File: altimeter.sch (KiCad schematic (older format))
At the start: 42 parts, among them Q101 DMG2301L, Q102 NTR4003NT1G, Q103 SISS05dn, U1 LMV331, U101 STM32F302CCTx, U102 S25FL512SAGMFIR11, U103 AIS2120SXTR, U104 MIC5219-3.3YM5, U105 LF50_TO252, U106 BMI088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

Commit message: first prototyp order
Signed-off-by: Thomas Schmid <tom@binary-kitchen.de>
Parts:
- removed D102: D_Zener, symbol Device:D_Zener
- added D102: LED, LED_SMD:LED_0603_1608Metric, symbol Device:LED
- R105: value 100k -> 680; Mouser_Link https://www.mouser.de/ProductDetail/Vishay-Dale/CRCW0402100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 -> https://www.mouser.de/ProductDetail/Vishay-Dale/CRCW0402680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; Parnumber CRCW0402100KFKEDC -> CRCW0402680RFKEDC
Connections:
- net +3V3: now also R105.2
- net GND: now also Q103.4 (G), D102.1 (K); no longer R105.2
- net at R105.1: now also D102.2 (A); no longer Q103.4 (G)
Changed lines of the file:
@@
 Connection ~ 7000 3200
 Wire Wire Line
-	8000 900  8000 1150
+	8000 900  8000 1050
 NoConn ~ 6300 3000
 NoConn ~ 6300 2800
@@
 Wire Wire Line
 	7550 1650 7550 1700
-Wire Wire Line
-	7550 1700 7400 1700
 $Comp
 L power:GND #PWR0164
 U 1 1 5D749A10
-P 7050 2550
-F 0 "#PWR0164" H 7050 2300 50  0001 C CNN
-F 1 "GND" H 7055 2377 50  0000 C CNN
-F 2 "" H 7050 2550 50  0001 C CNN
-F 3 "" H 7050 2550 50  0001 C CNN
-	1    7050 2550
-	1    0    0    -1
-$EndComp
-$Comp
-L Device:D_Zener D102
-U 1 1 5D74B84D
-P 7400 1900
-F 0 "D102" V 7446 1821 50  0000 R CNN
-F 1 "D_Zener" V 7355 1821 50  0000 R CNN
-F 2 "" H 7400 1900 50  0001 C CNN
-F 3 "~" H 7400 1900 50  0001 C CNN
-	1    7400 1900
-	0    -1   -1   0
-$EndComp
-$Comp
-L Device:R R105
-U 1 1 5D74CCF3
-P 7050 2300
-F 0 "R105" H 7120 2346 50  0000 L CNN
-F 1 "100k" H 7120 2255 50  0000 L CNN
-F 2 "Resistor_SMD:R_0402_1005Metric" V 6980 2300 50  0001 C CNN
-F 3 "~" H 7050 2300 50  0001 C CNN
-F 4 "https://www.mouser.de/ProductDetail/Vishay-Dale/CRCW0402100KFKED?qs=sGAEpiMZZMu61qfTUdNhG2DpbjADlD3GqPf2An0kBCw%3D" H 7050 2300 50  0001 C CNN "Mouser_Link"
-F 5 "CRCW0402100KFKEDC" H 7050 2300 50  0001 C CNN "Parnumber"
-	1    7050 2300
-	1    0    0    -1
-$EndComp
-Wire Wire Line
-	7050 2000 7050 2100
-Wire Wire Line
-	7050 2100 7400 2100
-Wire Wire Line
-	7400 2100 7400 2050
-Wire Wire Line
-	7400 1750 7400 1700
-Connection ~ 7400 1700
-Wire Wire Line
-	7400 1700 7250 1700
-Wire Wire Line
-	7050 2550 7050 2450
-Wire Wire Line
-	7050 2150 7050 2100
-Connection ~ 7050 2100
+P 7050 2150
+F 0 "#PWR0164" H 7050 1900 50  0001 C CNN
+F 1 "GND" H 7055 1977 50  0000 C CNN
+F 2 "" H 7050 2150 50  0001 C CNN
+F 3 "" H 7050 2150 50  0001 C CNN
+	1    7050 2150
+	1    0    0    -1
+$EndComp
 $Comp
 L altimeter:SI7149ADP Q103
@@
 $EndComp
 $Comp
-L power:VPP #PWR?
+L power:VPP #PWR0113
 U 1 1 5D715463
 P 2000 5150
-F 0 "#PWR?" H 2000 5000 50  0001 C CNN
+F 0 "#PWR0113" H 2000 5000 50  0001 C CNN
 F 1 "VPP" H 2015 5323 50  0000 C CNN
 F 2 "" H 2000 5150 50  0001 C CNN
@@
 $EndComp
 $Comp
-L power:VPP #PWR?
+L power:VPP #PWR0115
 U 1 1 5D715F7E
 P 9350 3300
-F 0 "#PWR?" H 9350 3150 50  0001 C CNN
+F 0 "#PWR0115" H 9350 3150 50  0001 C CNN
 F 1 "VPP" H 9365 3473 50  0000 C CNN
 F 2 "" H 9350 3300 50  0001 C CNN
@@
 $EndComp
 $Comp
-L power:VPP #PWR?
+L power:VPP #PWR0132
 U 1 1 5D7169CC
 P 8750 1000
-F 0 "#PWR?" H 8750 850 50  0001 C CNN
+F 0 "#PWR0132" H 8750 850 50  0001 C CNN
 F 1 "VPP" H 8765 1173 50  0000 C CNN
 F 2 "" H 8750 1000 50  0001 C CNN
@@
 	1    0    0    -1
 $EndComp
+Wire Wire Line
+	7050 2000 7050 2150
+Wire Wire Line
+	7250 1700 7550 1700
+$Comp
+L Device:R R105
+U 1 1 5D7330BE
+P 7250 1200
+F 0 "R105" V 7043 1200 50  0000 C CNN
+F 1 "680" V 7134 1200 50  0000 C CNN
+F 2 "Resistor_SMD:R_0402_1005Metric" V 7180 1200 50  0001 C CNN
+F 3 "~" H 7250 1200 50  0001 C CNN
+F 4 "https://www.mouser.de/ProductDetail/Vishay-Dale/CRCW0402680RFKED?qs=sGAEpiMZZMu61qfTUdNhG2DpbjADlD3GyuaBeN1cc%2FA%3D" H 7250 1200 50  0001 C CNN "Mouser_Link"
+F 5 "CRCW0402680RFKEDC" H 7250 1200 50  0001 C CNN "Parnumber"
+	1    7250 1200
+	0    1    1    0
+$EndComp
+$Comp
+L Device:LED D102
+U 1 1 5D733512
+P 7650 1200
+F 0 "D102" H 7643 945 50  0000 C CNN
+F 1 "LED" H 7643 1036 50  0000 C CNN
+F 2 "LED_SMD:LED_0603_1608Metric" H 7650 1200 50  0001 C CNN
+F 3 "~" H 7650 1200 50  0001 C CNN
+F 4 "https://www.mouser.de/ProductDetail/Kingbright/APTD1608LSURCK?qs=sGAEpiMZZMseGfSY3csMkdgyOOAg6kv2cxPgKHWlbm1IZYxSy1q3mw%3D%3D" H 7650 1200 50  0001 C CNN "Mouser_Link"
+F 5 "APTD1608LSURCK" H 7650 1200 50  0001 C CNN "Parnumber"
+	1    7650 1200
+	-1   0    0    1
+$EndComp
+Wire Wire Line
+	7400 1200 7500 1200
+Wire Wire Line
+	7800 1200 7900 1200
+Wire Wire Line
+	7900 1200 7900 1050
+Wire Wire Line
+	7900 1050 8000 1050
+Connection ~ 8000 1050
+Wire Wire Line
+	8000 1050 8000 1150
+$Comp
+L power:+3.3V #PWR0165
+U 1 1 5D74A821
+P 7100 1200
+F 0 "#PWR0165" H 7100 1050 50  0001 C CNN
+F 1 "+3.3V" V 7115 1328 50  0000 L CNN
+F 2 "" H 7100 1200 50  0001 C CNN
+F 3 "" H 7100 1200 50  0001 C CNN
+	1    7100 1200
+	0    -1   -1   0
+$EndComp
 $EndSCHEMATC

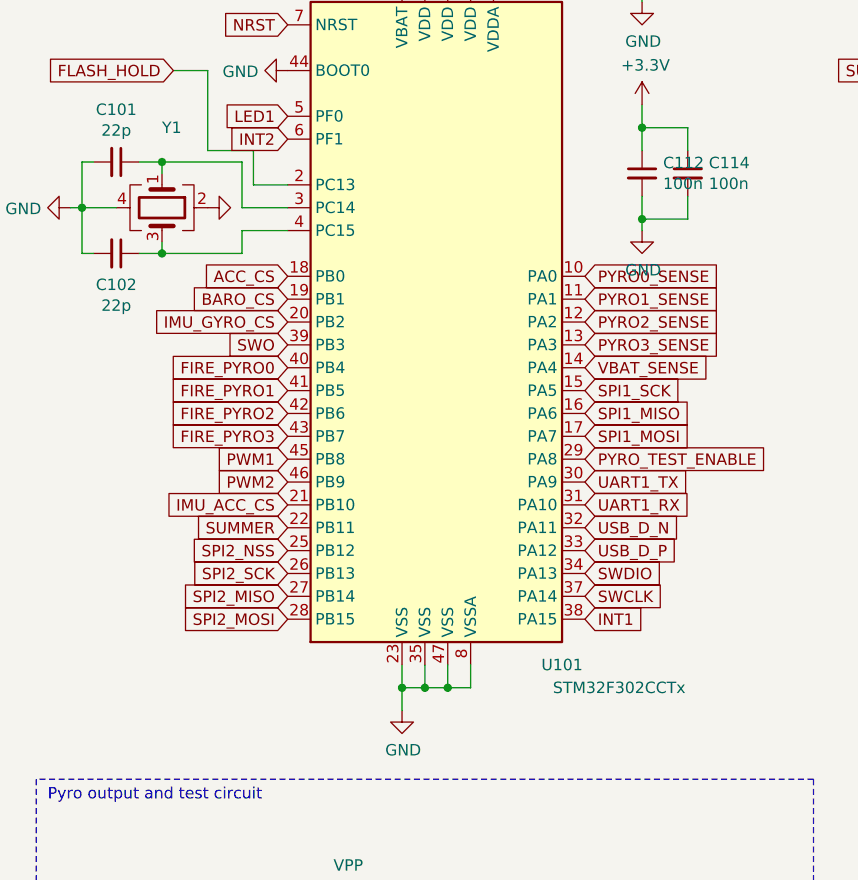
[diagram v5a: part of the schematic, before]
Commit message: changed mcu from stm32f302xc to stm32f303xc
Signed-off-by: Thomas Schmid <tom@binary-kitchen.de>
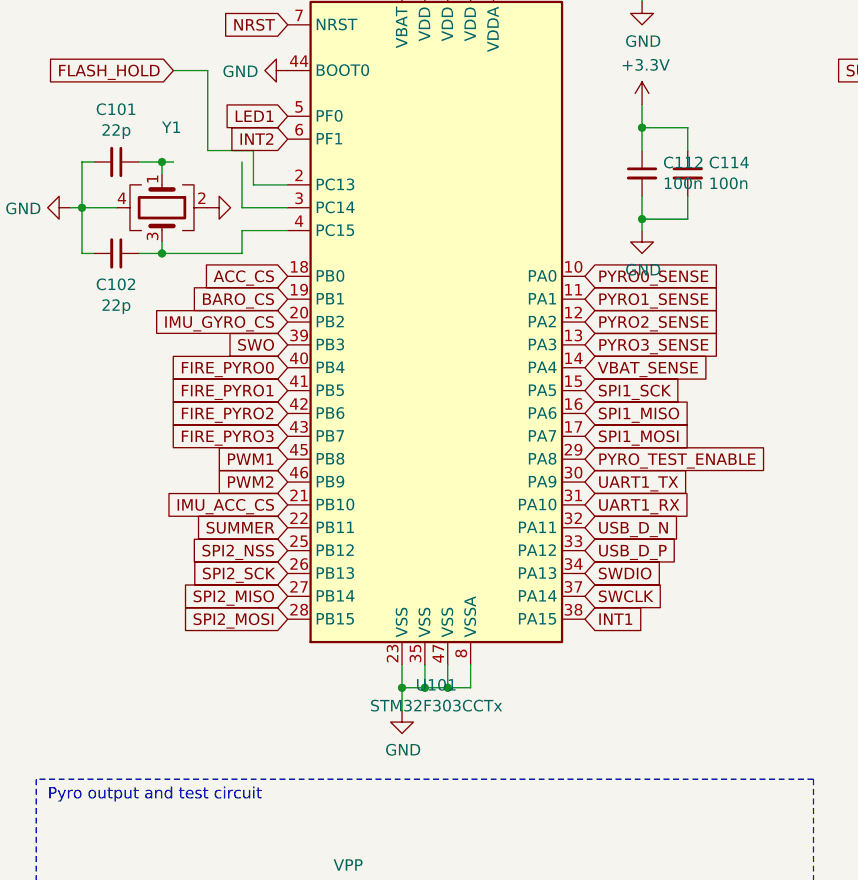
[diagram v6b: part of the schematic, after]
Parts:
- removed U101: STM32F302CCTx, Package_QFP:LQFP-48_7x7mm_P0.5mm, symbol MCU_ST_STM32F3:STM32F302CCTx
- added U101: STM32F303CCTx, Package_QFP:LQFP-48_7x7mm_P0.5mm, symbol MCU_ST_STM32F3:STM32F303CCTx
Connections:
- net +3V3: now also U101.1 (VBAT), U101.24 (VDD), U101.36 (VDD), U101.48 (VDD), U101.9 (VDDA)
- net ACC_CS: now also U101.18 (PB0)
- net BARO_CS: now also U101.19 (PB1)
- net FIRE_PYRO0: now also U101.40 (PB4)
- net FIRE_PYRO1: now also U101.41 (PB5)
- net FIRE_PYRO2: now also U101.42 (PB6)
- net FIRE_PYRO3: now also U101.43 (PB7)
- net FLASH_HOLD: now also U101.2 (PC13)
- net GND: now also U101.23 (VSS), U101.35 (VSS), U101.44 (BOOT0), U101.47 (VSS), U101.8 (VSSA)
- net IMU_ACC_CS: now also U101.21 (PB10)
- net IMU_GYRO_CS: now also U101.20 (PB2)
- net INT1: now also U101.38 (PA15)
- net INT2: now also U101.6 (PF1)
- net LED1: now also U101.5 (PF0)
- net NRST: now also U101.7 (NRST)
- net PWM1: now also U101.45 (PB8)
- net PWM2: now also U101.46 (PB9)
- net PYRO0_SENSE: now also U101.10 (PA0)
- net PYRO1_SENSE: now also U101.11 (PA1)
- net PYRO2_SENSE: now also U101.12 (PA2)
- net PYRO3_SENSE: now also U101.13 (PA3)
- net PYRO_TEST_ENABLE: now also U101.29 (PA8)
- net SPI1_MISO: now also U101.16 (PA6)
- net SPI1_MOSI: now also U101.17 (PA7)
- net SPI1_SCK: now also U101.15 (PA5)
- net SPI2_MISO: now also U101.27 (PB14)
- net SPI2_MOSI: now also U101.28 (PB15)
- net SPI2_NSS: now also U101.25 (PB12)
- net SPI2_SCK: now also U101.26 (PB13)
- net SUMMER: now also U101.22 (PB11)
- net SWCLK: now also U101.37 (PA14)
- net SWDIO: now also U101.34 (PA13)
- net SWO: now also U101.39 (PB3)
- net UART1_RX: now also U101.31 (PA10)
- net UART1_TX: now also U101.30 (PA9)
- net USB_D_N: now also U101.32 (PA11)
- net USB_D_P: now also U101.33 (PA12)
- net VBAT_SENSE: now also U101.14 (PA4)
- net at C102.1, Y1.3: now also U101.4 (PC15)
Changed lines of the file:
@@
 $EndDescr
-$Comp
-L MCU_ST_STM32F3:STM32F302CCTx U101
-U 1 1 5D3C66D6
-P 2450 2600
-F 0 "U101" H 2950 1100 50  0000 C CNN
-F 1 "STM32F302CCTx" H 3200 1000 50  0000 C CNN
-F 2 "Package_QFP:LQFP-48_7x7mm_P0.5mm" H 1850 1200 50  0001 R CNN
-F 3 "http://www.st.com/st-web-ui/static/active/en/resource/technical/document/datasheet/DM00094064.pdf" H 2450 2600 50  0001 C CNN
-F 4 "https://www.mouser.de/ProductDetail/STMicroelectronics/STM32F302CCT6?qs=sGAEpiMZZMuoKKEcg8mMKOBJ8oUHiKNHPcYeia7O8P4%3D" H 2450 2600 50  0001 C CNN "Mouser_Link"
-F 5 "STM32F302CCT6" H 2450 2600 50  0001 C CNN "Parnumber"
-	1    2450 2600
-	1    0    0    -1
-$EndComp
 $Comp
 L Sensor_Pressure:MS5611-01BA U107
@@
 Wire Wire Line
 	850  2100 1000 2100
-Wire Wire Line
-	1100 1900 1200 1900
 Connection ~ 1200 1900
 Wire Wire Line
@@
 	1550 1900 1550 2100
 Wire Wire Line
-	1200 1900 1550 1900
+	1200 1900 1250 1900
 Wire Wire Line
 	1550 2200 1550 2300
@@
 	0    -1   -1   0
 $EndComp
+$Comp
+L MCU_ST_STM32F3:STM32F303CCTx U101
+U 1 1 5D72F281
+P 2450 2600
+F 0 "U101" H 2400 1011 50  0000 C CNN
+F 1 "STM32F303CCTx" H 2400 920 50  0000 C CNN
+F 2 "Package_QFP:LQFP-48_7x7mm_P0.5mm" H 1850 1200 50  0001 R CNN
+F 3 "https://www.st.com/resource/en/datasheet/stm32f303cc.pdf" H 2450 2600 50  0001 C CNN
+F 4 "https://www.mouser.de/ProductDetail/STMicroelectronics/STM32F303CCT6?qs=sGAEpiMZZMts0YcPTleK%252BUygSfs3Z%2F6o" H 2450 2600 50  0001 C CNN "Mouser_Link"
+F 5 "STM32F303CCT6 " H 2450 2600 50  0001 C CNN "Parnumber"
+	1    2450 2600
+	1    0    0    -1
+$EndComp
+Wire Wire Line
+	1100 1900 1200 1900
 $EndSCHEMATC

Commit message: add some missing mouser links and part numbers to the schematic
Signed-off-by: Thomas Schmid <tom@binary-kitchen.de>
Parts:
- Q103: Mouser_Link (none) -> https://www.mouser.de/ProductDetail/Vishay-Siliconix/SISS05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; Parnumber (none) -> SISS05DN-T1-GE3
- R102: Mouser_Link (none) -> https://www.mouser.de/ProductDetail/Vishay-Dale/CRCW04022K7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
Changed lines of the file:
@@
 F 3 "~" H 10100 1150 50  0001 C CNN
 F 4 "CRCW04022K70FKEDC" H 10100 1150 50  0001 C CNN "Parnumber"
+F 5 "https://www.mouser.de/ProductDetail/Vishay-Dale/CRCW04022K70FKEDC?qs=sGAEpiMZZMu61qfTUdNhG9bvwnXh9sSrHB5zaMHoC9p2GBlct%252B1VIg%3D%3D" H 10100 1150 50  0001 C CNN "Mouser_Link"
 	1    10100 1150
 	1    0    0    -1
@@
 F 2 "Package_SO:Vishay_PowerPAK_1212-8_Single" H 7250 1900 50  0001 C CNN
 F 3 "https://www.mouser.de/datasheet/2/427/siss05dn-1595673.pdf" H 7050 1800 50  0001 C CNN
+F 4 "https://www.mouser.de/ProductDetail/Vishay-Siliconix/SISS05DN-T1-GE3?qs=%2Fha2pyFadugz6r8MF7HjV9XJLYucB9iA801wzI6YUU8%3D" H 7050 1800 50  0001 C CNN "Mouser_Link"
+F 5 "SISS05DN-T1-GE3" H 7050 1800 50  0001 C CNN "Parnumber"
 	1    7050 1800
 	0    -1   -1   0
